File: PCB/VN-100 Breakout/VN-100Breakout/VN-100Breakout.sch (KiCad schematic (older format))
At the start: 2 parts

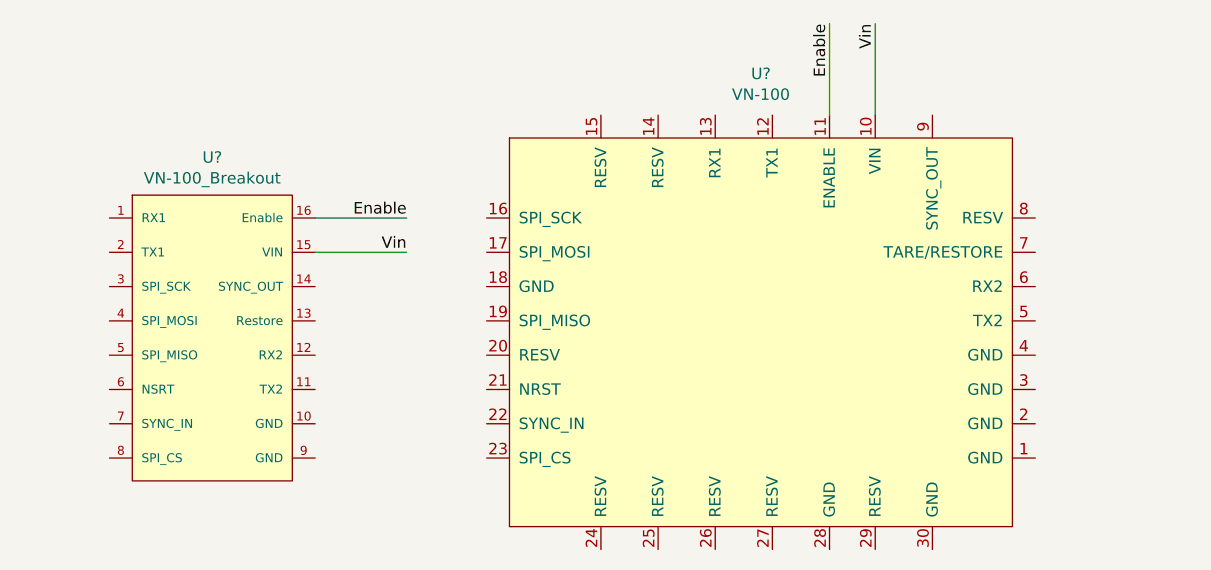
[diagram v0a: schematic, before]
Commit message: VN-100 Breakout  Created Label Connection
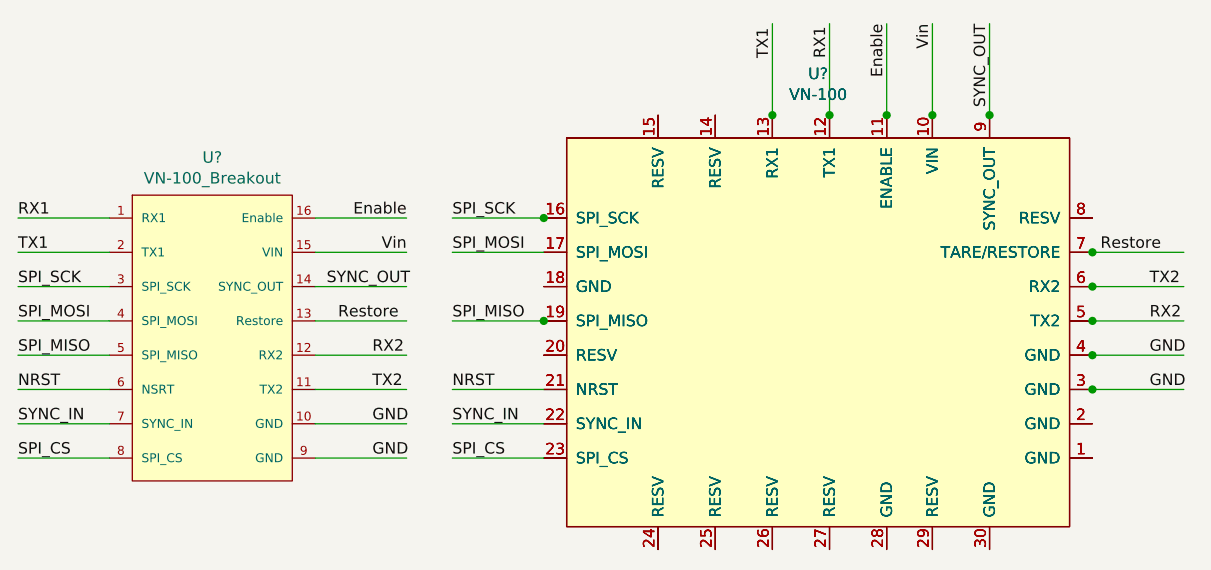
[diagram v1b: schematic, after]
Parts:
- added U?: VN-100, symbol PayloadSymbols:VN-100
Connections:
- net labels added: GND, NRST, RX1, RX2, Restore, SPI_CS, SPI_MISO, SPI_MOSI, SPI_SCK, SYNC_IN, SYNC_OUT, TX1, TX2
- wire segments 4 -> 32
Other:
- moved on the sheet: U?
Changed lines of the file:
@@
 L PayloadSymbols:VN-100 U?
 U 1 1 6163C870
-P 7150 4100
-F 0 "U?" H 7200 5331 50  0000 C CNN
-F 1 "VN-100" H 7200 5240 50  0000 C CNN
-F 2 "" H 6350 4600 50  0001 C CNN
-F 3 "" H 6350 4600 50  0001 C CNN
-	1    7150 4100
+P 7400 4100
+F 0 "U?" H 7450 5331 50  0000 C CNN
+F 1 "VN-100" H 7450 5240 50  0000 C CNN
+F 2 "" H 6600 4600 50  0001 C CNN
+F 3 "" H 6600 4600 50  0001 C CNN
+	1    7400 4100
 	1    0    0    -1
 $EndComp
@@
 Text Label 5650 3500 2    50   ~ 0
 Enable
-Wire Wire Line
-	7500 3050 7500 2650
-Text Label 7500 2650 3    50   ~ 0
+Text Label 7750 2650 3    50   ~ 0
 Enable
 Wire Wire Line
@@
 Text Label 5650 3650 2    50   ~ 0
 Vin
+Text Label 7950 2650 3    50   ~ 0
+Vin
 Wire Wire Line
-	7700 3050 7700 2650
-Text Label 7700 2650 3    50   ~ 0
-Vin
+	5250 3800 5650 3800
+Text Label 5300 3800 0    50   ~ 0
+SYNC_OUT
+Wire Wire Line
+	7750 2650 7750 3050
+Wire Wire Line
+	7950 2650 7950 3050
+Wire Wire Line
+	8200 2650 8200 3050
+Text Label 8200 2650 3    50   ~ 0
+SYNC_OUT
+Wire Wire Line
+	5250 3950 5650 3950
+Text Label 5350 3950 0    50   ~ 0
+Restore
+Wire Wire Line
+	9050 3650 8650 3650
+Text Label 8950 3650 2    50   ~ 0
+Restore
+Wire Wire Line
+	5250 4100 5650 4100
+Text Label 5500 4100 0    50   ~ 0
+RX2
+Wire Wire Line
+	8650 3950 9050 3950
+Text Label 8900 3950 0    50   ~ 0
+RX2
+Wire Wire Line
+	5250 4250 5650 4250
+Text Label 5500 4250 0    50   ~ 0
+TX2
+Wire Wire Line
+	8650 3800 9050 3800
+Text Label 8900 3800 0    50   ~ 0
+TX2
+Wire Wire Line
+	5250 4400 5650 4400
+Text Label 5500 4400 0    50   ~ 0
+GND
+Wire Wire Line
+	5250 4550 5650 4550
+Text Label 5500 4550 0    50   ~ 0
+GND
+Wire Wire Line
+	8650 4100 9050 4100
+Text Label 8900 4100 0    50   ~ 0
+GND
+Wire Wire Line
+	8650 4250 9050 4250
+Text Label 8900 4250 0    50   ~ 0
+GND
+Wire Wire Line
+	4350 3500 3950 3500
+Text Label 3950 3500 0    50   ~ 0
+RX1
+Wire Wire Line
+	7500 3050 7500 2650
+Text Label 7500 2800 1    50   ~ 0
+RX1
+Wire Wire Line
+	4350 3650 3950 3650
+Text Label 3950 3650 0    50   ~ 0
+TX1
+Wire Wire Line
+	7250 3050 7250 2650
+Text Label 7250 2800 1    50   ~ 0
+TX1
+Wire Wire Line
+	4350 3800 3950 3800
+Text Label 3950 3800 0    50   ~ 0
+SPI_SCK
+Wire Wire Line
+	6250 3500 5850 3500
+Text Label 5850 3500 0    50   ~ 0
+SPI_SCK
+Wire Wire Line
+	4350 3950 3950 3950
+Text Label 3950 3950 0    50   ~ 0
+SPI_MOSI
+$Comp
+L PayloadSymbols:VN-100 U?
+U 1 1 616483E5
+P 7400 4100
+F 0 "U?" H 7450 5331 50  0000 C CNN
+F 1 "VN-100" H 7450 5240 50  0000 C CNN
+F 2 "" H 6600 4600 50  0001 C CNN
+F 3 "" H 6600 4600 50  0001 C CNN
+	1    7400 4100
+	1    0    0    -1
+$EndComp
+Connection ~ 7950 3050
+Connection ~ 7750 3050
+Connection ~ 6250 3500
+Connection ~ 8650 4250
+Connection ~ 8650 4100
+Connection ~ 8650 3650
+Connection ~ 8200 3050
+Wire Wire Line
+	6250 3650 5850 3650
+Text Label 5850 3650 0    50   ~ 0
+SPI_MOSI
+Wire Wire Line
+	4350 4100 3950 4100
+Text Label 3950 4100 0    50   ~ 0
+SPI_MISO
+Wire Wire Line
+	6250 3950 5850 3950
+Text Label 5850 3950 0    50   ~ 0
+SPI_MISO
+Wire Wire Line
+	4350 4550 3950 4550
+Text Label 3950 4550 0    50   ~ 0
+SPI_CS
+Wire Wire Line
+	6250 4550 5850 4550
+Text Label 5850 4550 0    50   ~ 0
+SPI_CS
+Wire Wire Line
+	4350 4400 3950 4400
+Text Label 3950 4400 0    50   ~ 0
+SYNC_IN
+Wire Wire Line
+	6250 4400 5850 4400
+Text Label 5850 4400 0    50   ~ 0
+SYNC_IN
+Wire Wire Line
+	4350 4250 3950 4250
+Text Label 3950 4250 0    50   ~ 0
+NRST
+Wire Wire Line
+	6250 4250 5850 4250
+Connection ~ 6250 3950
+Connection ~ 7250 3050
+Connection ~ 7500 3050
+Text Label 5850 4250 0    50   ~ 0
+NRST
+Connection ~ 8650 3800
+Connection ~ 8650 3950
 $EndSCHEMATC
